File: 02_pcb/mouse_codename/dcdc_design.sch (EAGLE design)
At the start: 6 parts, among them IC1 STM32F405RGT6, IC2 MPU-6050, IC3 DRV88361

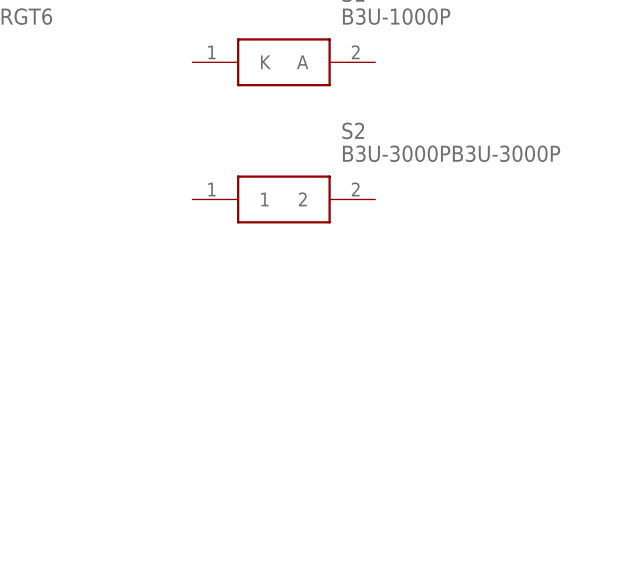
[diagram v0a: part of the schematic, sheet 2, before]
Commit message: eagle libraries updated, internal OC set with PLL
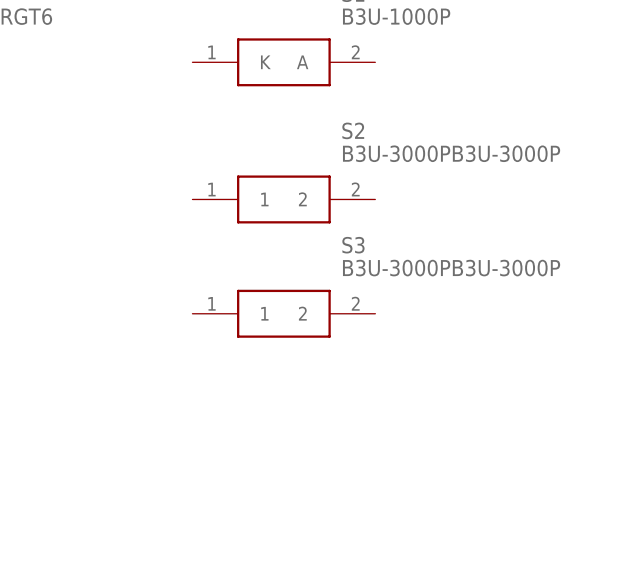
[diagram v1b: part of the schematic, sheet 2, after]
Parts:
- added S3: B3U-3000PB3U-3000P, parts:B3U-3000PB3U-3000P
- added U$1: JDY-10_STANDING, parts:JDY-10_STANDING
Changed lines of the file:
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@@
 <?xml version="1.0" encoding="utf-8"?>
 <!DOCTYPE eagle SYSTEM "eagle.dtd">
-<eagle version="9.3.0">
+<eagle version="9.3.1">
 <drawing>
 <settings>
@@
 <part name="IC1" library="parts" library_urn="urn:adsk.eagle:library:8879268" deviceset="STM32F405RGT6" device="" package3d_urn="urn:adsk.eagle:package:8879286/3"/>
 <part name="PS1" library="parts" library_urn="urn:adsk.eagle:library:8879268" deviceset="TPS82085" device="" package3d_urn="urn:adsk.eagle:package:8879285/3"/>
-<part name="IC3" library="parts" library_urn="urn:adsk.eagle:library:8879268" deviceset="DRV8836" device="1" package3d_urn="urn:adsk.eagle:package:8872076/3"/>
+<part name="IC3" library="parts" library_urn="urn:adsk.eagle:library:8879268" deviceset="DRV8836" device="1" package3d_urn="urn:adsk.eagle:package:8872076/4"/>
 <part name="IC2" library="parts" library_urn="urn:adsk.eagle:library:8879268" deviceset="MPU-6050" device="" package3d_urn="urn:adsk.eagle:package:8879287/3"/>
+<part name="U$1" library="parts" library_urn="urn:adsk.eagle:library:8879268" deviceset="JDY-10_STANDING" device="" package3d_urn="urn:adsk.eagle:package:8988323/2"/>
+<part name="S3" library="parts" library_urn="urn:adsk.eagle:library:8879268" deviceset="B3U-3000P" device="B3U-3000P" package3d_urn="urn:adsk.eagle:package:8879469/3"/>
 </parts>
 <sheets>
@@
 <attribute name="NAME" x="69.85" y="76.2" size="1.778" layer="95" align="center-left"/>
 <attribute name="VALUE" x="69.85" y="73.66" size="1.778" layer="96" align="center-left"/>
+</instance>
+<instance part="S3" gate="G$1" x="104.14" y="40.64" smashed="yes">
+<attribute name="NAME" x="120.65" y="48.26" size="1.778" layer="95" align="center-left"/>
+<attribute name="VALUE" x="120.65" y="45.72" size="1.778" layer="96" align="center-left"/>
 </instance>
 </instances>
@@
 </sheet>
 <sheet>
-<description>wifi modul</description>
+<description>wireless modul</description>
 <plain>
 </plain>
 <instances>
+<instance part="U$1" gate="G$1" x="45.72" y="53.34" smashed="yes"/>
 </instances>
 <busses>
